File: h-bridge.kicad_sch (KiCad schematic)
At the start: 20 parts, among them J4 Conn_02x06_Counter_Clockwise, M3 DC, Q10 Q_NMOS, Q7 Q_NMOS, Q8 Q_NMOS, Q9 Q_NMOS, U11 DRV8701

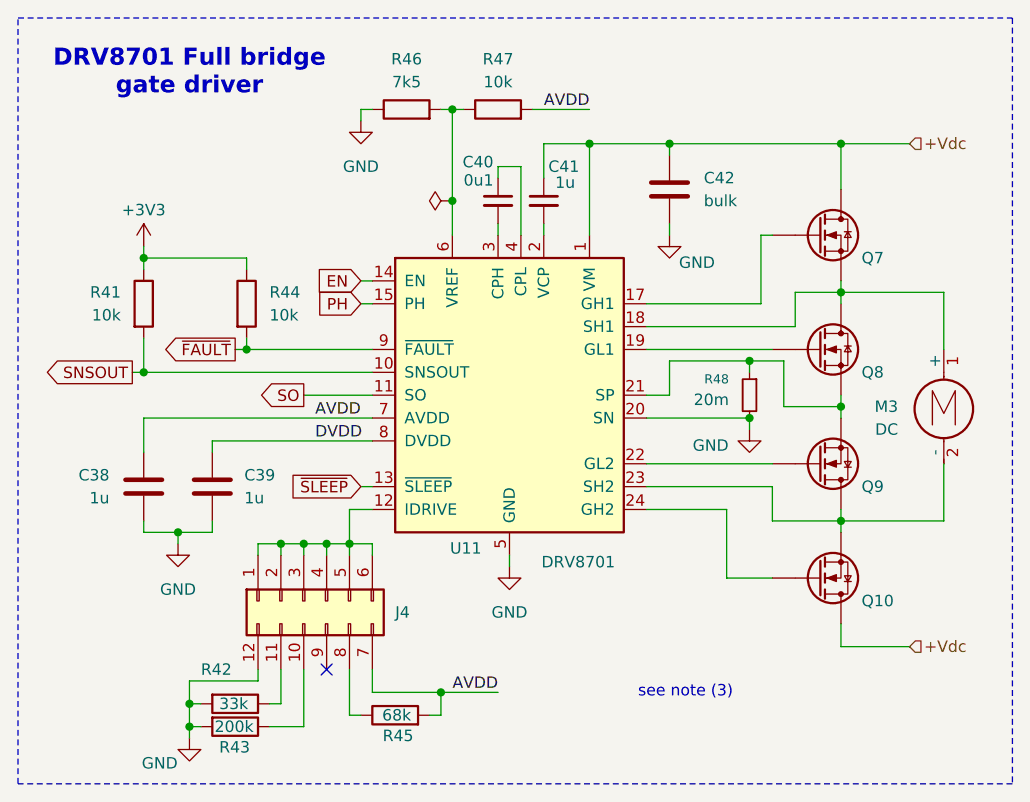
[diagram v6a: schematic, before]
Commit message: schem: assign footprints
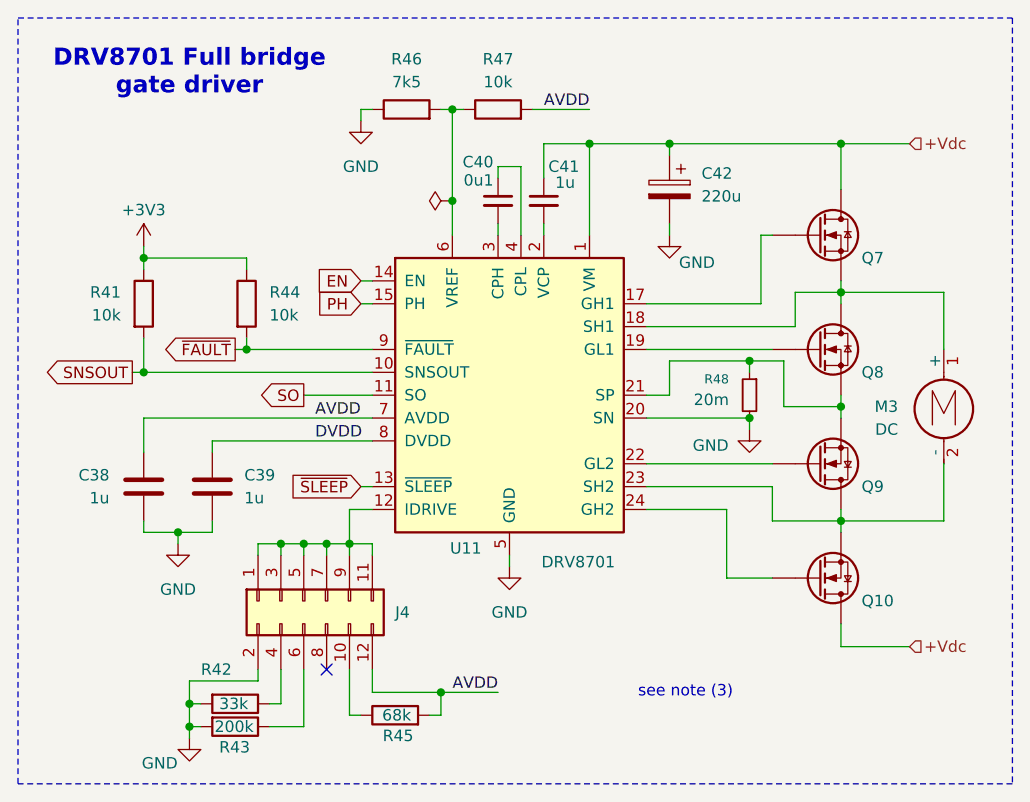
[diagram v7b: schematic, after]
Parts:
- removed C42: bulk, symbol Device:C
- added C42: 220u, Capacitor_SMD:CP_Elec_6.3x7.7, symbol Device:C_Polarized
- C38, C39, C40, C41: footprint (none) -> Capacitor_SMD:C_0402_1005Metric
- J4: footprint (none) -> Connector_PinHeader_2.54mm:PinHeader_2x06_P2.54mm_Vertical; symbol Connector_Generic:Conn_02x06_Counter_Clockwise -> Connector_Generic:Conn_02x06_Odd_Even
- Q10, Q7, Q8, Q9: footprint (none) -> Package_SO:Vishay_PowerPAK_1212-8_Single
- R41, R42, R43, R44, R45, R46, R47: footprint (none) -> Resistor_SMD:R_0402_1005Metric
- R48: footprint (none) -> Resistor_SMD:R_2512_6332Metric
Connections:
- net +Vdc: now also C42.1
- net AVDD: now also J4.12 (Pin_12); no longer J4.7 (Pin_7)
- net GND: now also J4.2 (Pin_2), C42.2; no longer J4.12 (Pin_12)
- net at R43.1: now also J4.6 (Pin_6); no longer J4.10 (Pin_10)
- net at R45.1: now also J4.10 (Pin_10); no longer J4.8 (Pin_8)
- net at J4.1 (Pin_1), J4.3 (Pin_3), J4.5 (Pin_5)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: now also J4.11 (Pin_11), J4.7 (Pin_7), J4.9 (Pin_9); no longer J4.2 (Pin_2), J4.4 (Pin_4), J4.6 (Pin_6)
- net at R42.1: now also J4.4 (Pin_4); no longer J4.11 (Pin_11)
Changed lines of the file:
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@@
 			)
 		)
-		(property "Footprint" ""
+		(property "Footprint" "Resistor_SMD:R_0402_1005Metric"
 			(at 146.05 56.388 90)
 			(effects
@@
 			)
 		)
-		(property "Footprint" ""
+		(property "Footprint" "Capacitor_SMD:C_0402_1005Metric"
 			(at 107.6452 100.33 0)
 			(effects
@@
 			)
 		)
-		(property "Footprint" ""
+		(property "Footprint" "Resistor_SMD:R_0402_1005Metric"
 			(at 116.84 121.412 90)
 			(effects
@@
 			)
 		)
-		(property "Footprint" ""
+		(property "Footprint" "Package_SO:Vishay_PowerPAK_1212-8_Single"
 			(at 186.69 66.04 0)
 			(effects
@@
 			)
 		)
-		(property "Footprint" ""
+		(property "Footprint" "Capacitor_SMD:C_0402_1005Metric"
 			(at 113.3348 100.33 0)
 			(effects
@@
 			)
 		)
-		(property "Footprint" ""
+		(property "Footprint" "Capacitor_SMD:C_0402_1005Metric"
 			(at 151.13 64.77 0)
 			(effects
@@
 			)
 		)
-		(property "Footprint" ""
+		(property "Footprint" "Resistor_SMD:R_0402_1005Metric"
 			(at 135.89 56.388 90)
 			(effects
@@
 	)
 	(symbol
-		(lib_id "Device:C")
+		(lib_id "Device:C_Polarized")
 		(at 165.1 63.5 0)
 		(mirror y)
@@
 		(on_board yes)
 		(dnp no)
-		(fields_autoplaced yes)
 		(property "Reference" "C42"
-			(at 168.91 62.2299 0)
+			(at 168.656 61.722 0)
 			(effects
 				(font
@@
 			)
 		)
-		(property "Value" "bulk"
-			(at 168.91 64.7699 0)
+		(property "Value" "220u"
+			(at 168.656 64.262 0)
 			(effects
 				(font
@@
 			)
 		)
-		(property "Footprint" ""
+		(property "Footprint" "Capacitor_SMD:CP_Elec_6.3x7.7"
 			(at 164.1348 67.31 0)
 			(effects
@@
 			)
 		)
-		(property "Description" "Unpolarized capacitor"
+		(property "Description" "Polarized capacitor"
 			(at 165.1 63.5 0)
 			(effects
@@
 			)
 		)
-		(pin "1"
+		(property "Basic" "X"
+			(at 165.1 63.5 0)
+			(effects
+				(font
+					(size 1.27 1.27)
+				)
+				(hide yes)
+			)
+		)
+		(property "JLCPCB Part #" "C46550411"
+			(at 165.1 63.5 0)
+			(effects
+				(font
+					(size 1.27 1.27)
+				)
+				(hide yes)
+			)
+		)
+		(property "Manufacturer" "jieerrui"
+			(at 165.1 63.5 0)
+			(effects
+				(font
+					(size 1.27 1.27)
+				)
+				(hide yes)
+			)
+		)
+		(property "Manufacturer Part Number" "JVJ35V220M6x8"
+			(at 165.1 63.5 0)
+			(effects
+				(font
+					(size 1.27 1.27)
+				)
+				(hide yes)
+			)
 		)
 		(pin "2"
+		)
+		(pin "1"
 		)
 		(instances
@@
 			)
 		)
-		(property "Footprint" ""
+		(property "Footprint" "Resistor_SMD:R_2512_6332Metric"
 			(at 173.99 86.36 0)
 			(effects
@@
 			)
 		)
-		(property "Footprint" ""
+		(property "Footprint" "Resistor_SMD:R_0402_1005Metric"
 			(at 134.62 123.698 90)
 			(effects
@@
 	)
 	(symbol
-		(lib_id "Connector_Generic:Conn_02x06_Counter_Clockwise")
+		(lib_id "Connector_Generic:Conn_02x06_Odd_Even")
 		(at 124.46 109.22 90)
 		(mirror x)
@@
 			)
 		)
-		(property "Footprint" ""
+		(property "Footprint" "Connector_PinHeader_2.54mm:PinHeader_2x06_P2.54mm_Vertical"
 			(at 124.46 109.22 0)
 			(effects
@@
 			)
 		)
-		(property "Description" "Generic connector, double row, 02x06, counter clockwise pin numbering scheme (similar to DIP package numbering), script generated (kicad-library-utils/schlib/autogen/connector/)"
+		(property "Description" "Generic connector, double row, 02x06, odd/even pin numbering scheme (row 1 odd numbers, row 2 even numbers), script generated (kicad-library-utils/schlib/autogen/connector/)"
 			(at 124.46 109.22 0)
 			(effects
@@
 			)
 		)
-		(property "Footprint" ""
+		(property "Footprint" "Resistor_SMD:R_0402_1005Metric"
 			(at 116.84 118.872 90)
 			(effects
@@
 			)
 		)
-		(property "Footprint" ""
+		(property "Footprint" "Resistor_SMD:R_0402_1005Metric"
 			(at 116.332 76.2 90)
 			(effects
@@
 			)
 		)
-		(property "Footprint" ""
+		(property "Footprint" "Package_SO:Vishay_PowerPAK_1212-8_Single"
 			(at 186.69 96.52 0)
 			(effects
@@
 			)
 		)
-		(property "Footprint" ""
+		(property "Footprint" "Capacitor_SMD:C_0402_1005Metric"
 			(at 146.05 64.77 0)
 			(effects
@@
 			)
 		)
-		(property "Footprint" ""
+		(property "Footprint" "Package_SO:Vishay_PowerPAK_1212-8_Single"
 			(at 186.69 109.22 0)
 			(effects
@@
 			)
 		)
-		(property "Footprint" ""
+		(property "Footprint" "Package_SO:Vishay_PowerPAK_1212-8_Single"
 			(at 186.69 78.74 0)
 			(effects
@@
 			)
 		)
-		(property "Footprint" ""
+		(property "Footprint" "Resistor_SMD:R_0402_1005Metric"
 			(at 104.902 76.2 90)
 			(effects

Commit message: schem: add connectors footprint
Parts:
- M3: footprint (none) -> TerminalBlock_Phoenix:TerminalBlock_Phoenix_MKDS-1,5-2-5.08_1x02_P5.08mm_Horizontal
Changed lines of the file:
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@@
 			)
 		)
-		(property "Footprint" ""
+		(property "Footprint" "TerminalBlock_Phoenix:TerminalBlock_Phoenix_MKDS-1,5-2-5.08_1x02_P5.08mm_Horizontal"
 			(at 195.58 88.646 0)
 			(effects
